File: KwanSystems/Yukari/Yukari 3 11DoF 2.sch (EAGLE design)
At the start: 63 parts, among them J003 M06, J301 JST 2mm, J406 11DoF, J501 GP-2106, J600 M02PTH, U101 BMP180, U201 5319, U301 73831, U401 LPC2148, U501 5319 1.8V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

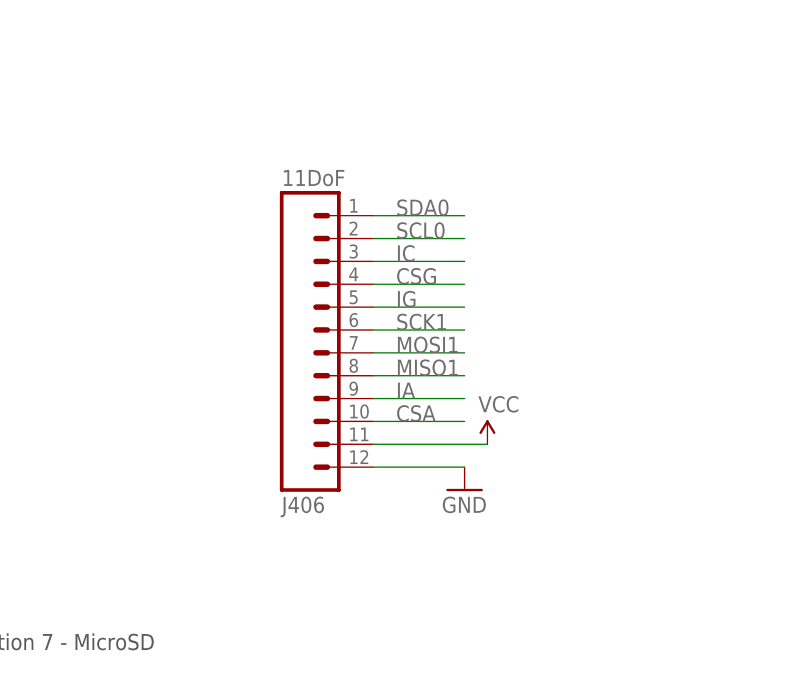
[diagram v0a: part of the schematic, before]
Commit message: Added Yukari4, changed it over to use templates
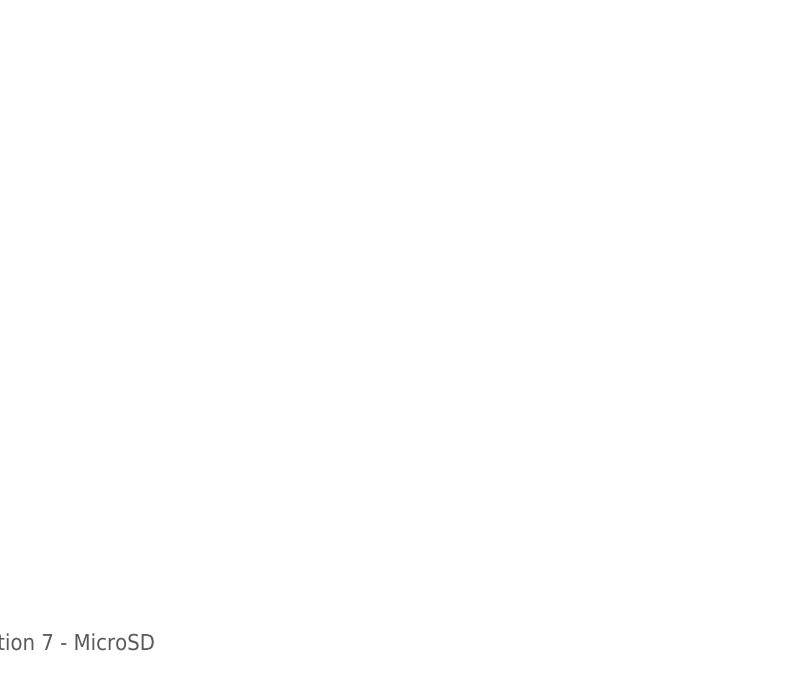
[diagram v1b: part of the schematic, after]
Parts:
- removed J406: 11DoF, SparkFun:M12PTH
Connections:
- removed net CSA: J406.10
- removed net CSG: J406.4
- removed net IC: J406.3
- removed net IG: J406.5
- removed net MISO1: J406.8
- removed net MOSI1: J406.7
- removed net SCK1: J406.6
- net GND: no longer J406.12
- net IA: no longer J406.9
- net SCL0: no longer J406.2
- net SDA0: no longer J406.1
- net VCC: no longer J406.11
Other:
- note removed: "3V3"
- note removed: "CSA"
- note removed: "CSG"
- note removed: "IA"
- note removed: "IC"
- note removed: "IG"
- note removed: "MISO"
- note removed: "MOSI"
- note removed: "SCK"
- note removed: "SCL"
- note removed: "SDA"
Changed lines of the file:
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@@
 <?xml version="1.0" encoding="utf-8"?>
 <!DOCTYPE eagle SYSTEM "eagle.dtd">
-<eagle version="6.5.0">
+<eagle version="7.3.0">
 <drawing>
 <settings>
@@
 <part name="JP5" library="SparkFun-Connectors" deviceset="M04" device="PTH"/>
 <part name="JP6" library="SparkFun-Connectors" deviceset="M04" device="PTH"/>
-<part name="J406" library="SparkFun" deviceset="M12" device="PTH" value="11DoF"/>
-<part name="P+8" library="SparkFun" deviceset="VCC" device=""/>
-<part name="GND2" library="SparkFun" deviceset="GND" device=""/>
 </parts>
 <sheets>
@@
 <text x="292.1" y="104.14" size="1.778" layer="97">Section 6 - 9DoF sensor</text>
 <text x="325.12" y="129.54" size="1.778" layer="97">Section 1 - Baro/Temp sensor</text>
-<text x="292.1" y="187.96" size="1.778" layer="98" align="center-right">GND</text>
-<text x="292.1" y="190.5" size="1.778" layer="98" align="center-right">3V3</text>
-<text x="292.1" y="193.04" size="1.778" layer="98" align="center-right">CSA</text>
-<text x="292.1" y="195.58" size="1.778" layer="98" align="center-right">IA</text>
-<text x="292.1" y="198.12" size="1.778" layer="98" align="center-right">MISO</text>
-<text x="292.1" y="200.66" size="1.778" layer="98" align="center-right">MOSI</text>
-<text x="292.1" y="203.2" size="1.778" layer="98" align="center-right">SCK</text>
-<text x="292.1" y="205.74" size="1.778" layer="98" align="center-right">IG</text>
-<text x="292.1" y="208.28" size="1.778" layer="98" align="center-right">CSG</text>
-<text x="292.1" y="210.82" size="1.778" layer="98" align="center-right">IC</text>
-<text x="292.1" y="213.36" size="1.778" layer="98" align="center-right">SCL</text>
-<text x="292.1" y="215.9" size="1.778" layer="98" align="center-right">SDA</text>
 </plain>
 <instances>
@@
 <instance part="JP5" gate="G$1" x="-53.34" y="71.12" rot="MR0"/>
 <instance part="JP6" gate="G$1" x="-43.18" y="71.12"/>
-<instance part="J406" gate="G$1" x="292.1" y="200.66" rot="MR180"/>
-<instance part="P+8" gate="1" x="314.96" y="190.5"/>
-<instance part="GND2" gate="1" x="312.42" y="185.42"/>
 </instances>
 <busses>
@@
 <wire x1="-63.5" y1="76.2" x2="-58.42" y2="76.2" width="0.1524" layer="91"/>
 <pinref part="JP5" gate="G$1" pin="4"/>
-</segment>
-<segment>
-<wire x1="302.26" y1="190.5" x2="314.96" y2="190.5" width="0.1524" layer="91"/>
-<pinref part="J406" gate="G$1" pin="11"/>
-<pinref part="P+8" gate="1" pin="VCC"/>
 </segment>
 </net>
@@
 <wire x1="236.22" y1="-15.24" x2="215.9" y2="-15.24" width="0.1524" layer="91"/>
 </segment>
-<segment>
-<wire x1="302.26" y1="187.96" x2="312.42" y2="187.96" width="0.1524" layer="91"/>
-<pinref part="J406" gate="G$1" pin="12"/>
-<pinref part="GND2" gate="1" pin="GND"/>
-</segment>
 </net>
 <net name="VBUS" class="1">
@@
 <pinref part="U601" gate="G$1" pin="SDA"/>
 </segment>
-<segment>
-<wire x1="302.26" y1="215.9" x2="312.42" y2="215.9" width="0.1524" layer="91"/>
-<label x="304.8" y="215.9" size="1.778" layer="95"/>
-<pinref part="J406" gate="G$1" pin="1"/>
-</segment>
 </net>
 <net name="SCL0" class="0">
@@
 <label x="325.12" y="93.98" size="1.778" layer="95"/>
 <pinref part="U601" gate="G$1" pin="SCL"/>
-</segment>
-<segment>
-<wire x1="302.26" y1="213.36" x2="312.42" y2="213.36" width="0.1524" layer="91"/>
-<label x="304.8" y="213.36" size="1.778" layer="95"/>
-<pinref part="J406" gate="G$1" pin="2"/>
 </segment>
 </net>
@@
 <pinref part="U601" gate="G$1" pin="INT"/>
 </segment>
-<segment>
-<wire x1="302.26" y1="195.58" x2="312.42" y2="195.58" width="0.1524" layer="91"/>
-<label x="304.8" y="195.58" size="1.778" layer="95"/>
-<pinref part="J406" gate="G$1" pin="9"/>
-</segment>
 </net>
 <net name="N$2" class="0">
@@
 </segment>
 </net>
-<net name="MISO1" class="0">
-<segment>
-<wire x1="302.26" y1="198.12" x2="312.42" y2="198.12" width="0.1524" layer="91"/>
-<label x="304.8" y="198.12" size="1.778" layer="95"/>
-<pinref part="J406" gate="G$1" pin="8"/>
-</segment>
-</net>
-<net name="MOSI1" class="0">
-<segment>
-<wire x1="302.26" y1="200.66" x2="312.42" y2="200.66" width="0.1524" layer="91"/>
-<label x="304.8" y="200.66" size="1.778" layer="95"/>
-<pinref part="J406" gate="G$1" pin="7"/>
-</segment>
-</net>
-<net name="SCK1" class="0">
-<segment>
-<wire x1="302.26" y1="203.2" x2="312.42" y2="203.2" width="0.1524" layer="91"/>
-<label x="304.8" y="203.2" size="1.778" layer="95"/>
-<pinref part="J406" gate="G$1" pin="6"/>
-</segment>
-</net>
-<net name="CSG" class="0">
-<segment>
-<wire x1="302.26" y1="208.28" x2="312.42" y2="208.28" width="0.1524" layer="91"/>
-<label x="304.8" y="208.28" size="1.778" layer="95"/>
-<pinref part="J406" gate="G$1" pin="4"/>
-</segment>
-</net>
-<net name="CSA" class="0">
-<segment>
-<wire x1="302.26" y1="193.04" x2="312.42" y2="193.04" width="0.1524" layer="91"/>
-<label x="304.8" y="193.04" size="1.778" layer="95"/>
-<pinref part="J406" gate="G$1" pin="10"/>
-</segment>
-</net>
-<net name="IG" class="0">
-<segment>
-<wire x1="302.26" y1="205.74" x2="312.42" y2="205.74" width="0.1524" layer="91"/>
-<label x="304.8" y="205.74" size="1.778" layer="95"/>
-<pinref part="J406" gate="G$1" pin="5"/>
-</segment>
-</net>
-<net name="IC" class="0">
-<segment>
-<wire x1="302.26" y1="210.82" x2="312.42" y2="210.82" width="0.1524" layer="91"/>
-<label x="304.8" y="210.82" size="1.778" layer="95"/>
-<pinref part="J406" gate="G$1" pin="3"/>
-</segment>
-</net>
